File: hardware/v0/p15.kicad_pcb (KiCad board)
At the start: 2 copper layers, 95.2 x 95.2 mm, 97 parts, among them J2 USB4105-GF-A, SW1 SW_Push, U1 ATmega32U4-AU, U2 TPD4EUSB30, Y1 16MHz

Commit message: move things around
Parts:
- moved Y1 24.2 mm to (95.2, 66.7)

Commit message: Conect crystal
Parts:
- moved D0,3 38.1 mm to (119.1, 50.0)
- moved C8 22.8 mm to (96.5, 64.7), turned to -45 degrees
- moved C7 19.8 mm to (90.8, 68.5), turned to -45 degrees
- moved Y1 3.21 mm to (92.3, 65.4), turned to 135 degrees
- moved C1 2.39 mm to (80.3, 46.5)
- moved C2 2.39 mm to (93.1, 45.2)
- moved F1 2.39 mm to (90.7, 45.2)
- moved R5 2.39 mm to (81.2, 49.5)
- moved R3 2.39 mm to (85.0, 46.5)
- moved U2 2.39 mm to (86.0, 42.9)
- moved J2 2.38 mm to (85.7, 35.7)
- turned D0,1 to 0 degrees
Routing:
- net /xTall2: track 0.00 -> 7.00 mm
- net /xTall1: track 0.00 -> 4.97 mm
- net Net-(D0,1-Pad2): track 0.00 -> 1.96 mm

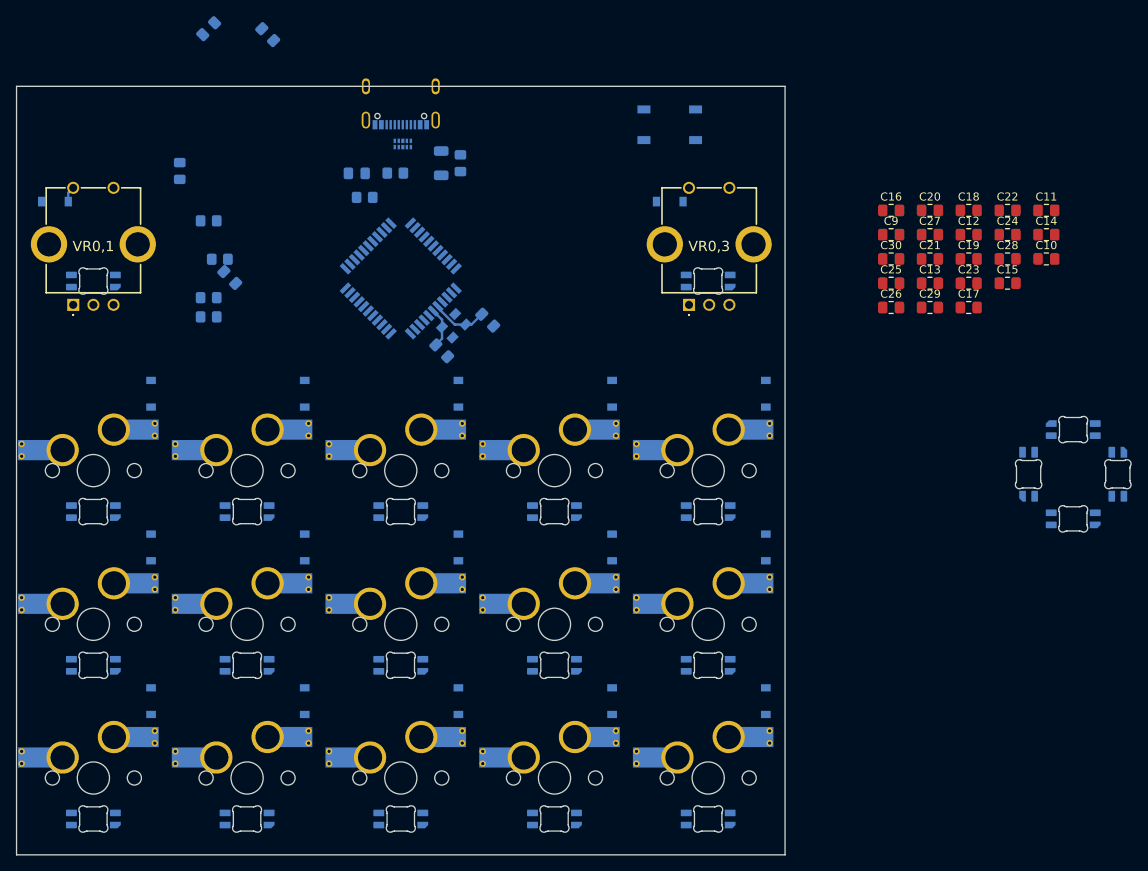
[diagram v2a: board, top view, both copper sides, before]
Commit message: routed crytal
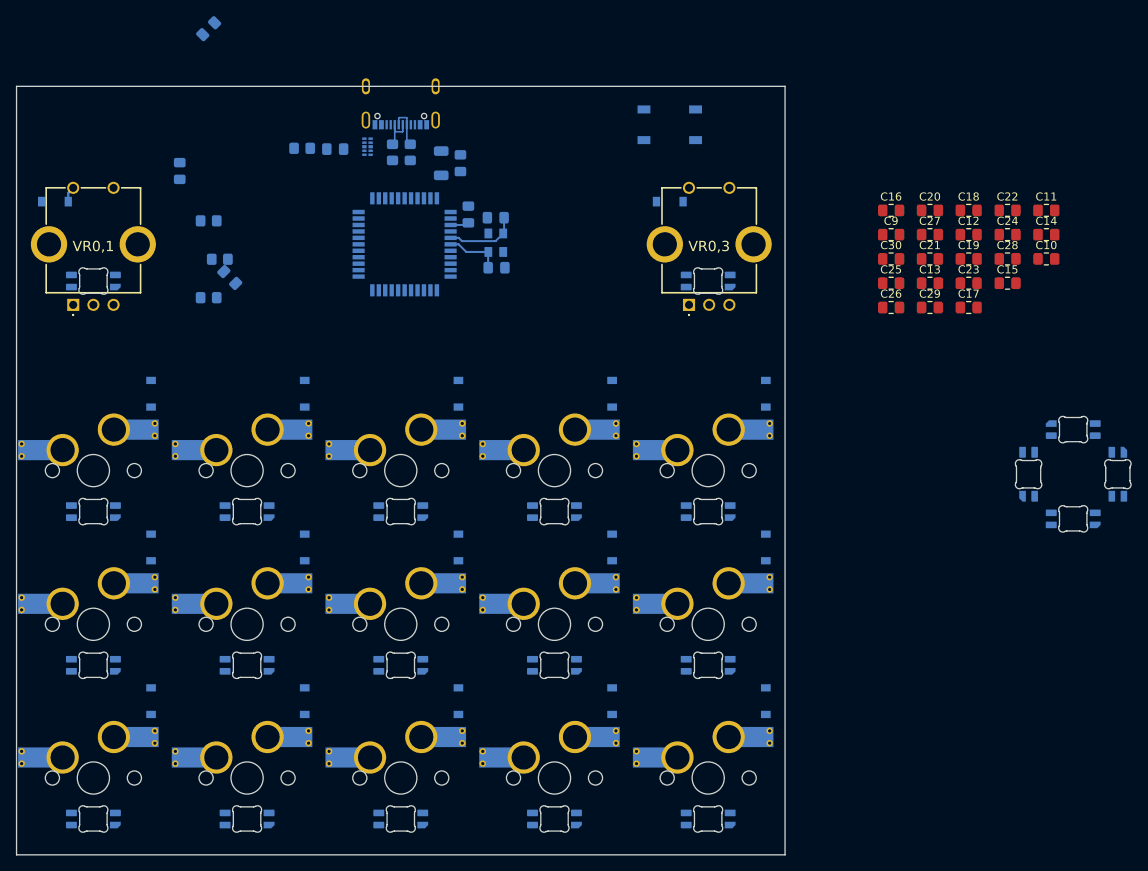
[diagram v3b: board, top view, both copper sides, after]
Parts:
- moved C3 33.4 mm to (94.1, 51.6), turned to 90 degrees
- moved R4 30.6 mm to (84.7, 43.9), turned to -90 degrees
- moved C8 12.7 mm to (97.5, 52.0), turned to 180 degrees
- moved C7 12.3 mm to (97.6, 58.2), turned to 0 degrees
- moved Y1 11.5 mm to (97.5, 55.1), turned to 180 degrees
- moved R5 9.85 mm to (73.5, 43.4)
- moved U2 4.39 mm to (81.6, 43.2), turned to 180 degrees
- moved U1 4.26 mm to (86.2, 55.3), turned to -90 degrees
- moved C1 4.02 mm to (77.6, 43.5)
- moved R3 3.17 mm to (86.9, 43.9), turned to -90 degrees
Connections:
- R3 pad 2: Net-(R3-Pad2) -> D+
- R4 pad 2: Net-(R4-Pad2) -> D-
- U1 pad 3: Net-(R4-Pad2) -> D-
- U1 pad 4: Net-(R3-Pad2) -> D+
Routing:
- net D+: track 0.00 -> 5.29 mm
- net D-: track 0.00 -> 5.22 mm
- net +5V: track 0.00 -> 2.31 mm
- net /xTall2: track 7.00 -> 9.08 mm
- net /xTall1: track 4.97 -> 7.04 mm

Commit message: more routing
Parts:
- added C31: 100n, Capacitor_SMD:C_0805_2012Metric_Pad1.18x1.45mm_HandSolder, B.Cu at (84.7, 49.2)
- added C32: 100n, Capacitor_SMD:C_0805_2012Metric_Pad1.18x1.45mm_HandSolder, B.Cu at (93.4, 65.2)
- moved C6 35.7 mm to (91.0, 49.3), turned to 0 degrees
- moved C5 23.4 mm to (80.4, 53.9), turned to -90 degrees
- moved C4 16.0 mm to (80.5, 60.2), turned to 90 degrees
- moved C1 13.1 mm to (90.2, 47.0), turned to 0 degrees
- moved F1 6.45 mm to (96.7, 42.8)
- moved C2 6.45 mm to (99.1, 42.8)
- moved C7 4.28 mm to (101.0, 60.8)
- moved Y1 4.12 mm to (101.1, 57.1), turned to -135 degrees
- moved C8 3.75 mm to (101.0, 53.3)
- moved C3 3.54 mm to (97.1, 53.5)
- moved U1 3.54 mm to (89.2, 57.2)
- moved R4 0.45 mm to (84.9, 43.5)
- moved R3 0.41 mm to (86.9, 43.5)
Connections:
- U1 pad 42: unconnected-(U1-Pad42) -> +5V
- U1 pad 7: unconnected-(U1-Pad7) -> +5V
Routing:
- net D+: track 5.29 -> 19.8 mm
- net D-: track 5.22 -> 16.5 mm
- net /xTall2: track 9.08 -> 0.00 mm
- net /xTall1: track 7.04 -> 0.00 mm

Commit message: last changes not sure what
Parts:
- moved C9 109.6 mm to (41.8, 86.4)
- moved C26 0.10 mm to (146.6, 63.1)
